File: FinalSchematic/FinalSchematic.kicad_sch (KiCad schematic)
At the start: 67 parts, among them M1 Pololu 4752, Q1 IRLZ44N, U1 OPA2197xD, U10 LM7912CT, U11 MEA1D1215SC, U12 OPA2197xD, U13 XR2206CP-F, U2 OPA2197xD, U3 OPA2197xD, U4 OPA2197xD, U5 LM311, U6 MCP1407-E_SN, U7 LM2917MX-8_NOPB, U8 OPA2197xD, U9 LM7812CT

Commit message: updated schematic
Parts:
- added RSHUNT: 1, symbol Device:R_US
- C11, C9: value 0.1u -> 1u
- C5: value 0.1u -> 0.027u
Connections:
- net GND: now also RSHUNT.1; no longer Q1.3 (S)
- new net: Q1.3 (S), RSHUNT.2
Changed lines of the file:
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@@
 	(wire
 		(pts
-			(xy 90.17 172.72) (xy 90.17 171.45)
-		)
-		(stroke
-			(width 0)
-			(type default)
-		)
-	)
-	(wire
-		(pts
 			(xy 127 76.2) (xy 124.46 76.2)
 		)
@@
 			)
 		)
-		(property "Value" "0.1u"
+		(property "Value" "0.027u"
 			(at 133.35 101.6 90)
 			(effects
@@
 	)
 	(symbol
+		(lib_id "Device:R_US")
+		(at 90.17 175.26 180)
+		(unit 1)
+		(exclude_from_sim no)
+		(in_bom yes)
+		(on_board yes)
+		(dnp no)
+		(fields_autoplaced yes)
+		(property "Reference" "RSHUNT"
+			(at 92.71 173.9899 0)
+			(effects
+				(font
+					(size 1.27 1.27)
+				)
+				(justify right)
+			)
+		)
+		(property "Value" "1"
+			(at 92.71 176.5299 0)
+			(effects
+				(font
+					(size 1.27 1.27)
+				)
+				(justify right)
+			)
+		)
+		(property "Footprint" ""
+			(at 89.154 175.006 90)
+			(effects
+				(font
+					(size 1.27 1.27)
+				)
+				(hide yes)
+			)
+		)
+		(property "Datasheet" "~"
+			(at 90.17 175.26 0)
+			(effects
+				(font
+					(size 1.27 1.27)
+				)
+				(hide yes)
+			)
+		)
+		(property "Description" "Resistor, US symbol"
+			(at 90.17 175.26 0)
+			(effects
+				(font
+					(size 1.27 1.27)
+				)
+				(hide yes)
+			)
+		)
+		(pin "2"
+		)
+		(pin "1"
+		)
+		(instances
+			(project "FinalSchematic"
+				(path "/3fb329af-5fd6-422e-bf74-f8f2d2cf8848"
+					(reference "RSHUNT")
+					(unit 1)
+				)
+			)
+		)
+	)
+	(symbol
 		(lib_id "Device:C_US")
 		(at 60.96 153.67 0)
@@
 			)
 		)
-		(property "Value" "0.1u"
+		(property "Value" "1u"
 			(at 265.43 134.112 90)
 			(effects
@@
 	(symbol
 		(lib_id "power:GND")
-		(at 90.17 172.72 0)
+		(at 90.17 179.07 0)
 		(unit 1)
 		(exclude_from_sim no)
@@
 		(fields_autoplaced yes)
 		(property "Reference" "#PWR016"
-			(at 90.17 179.07 0)
+			(at 90.17 185.42 0)
 			(effects
 				(font
@@
 		)
 		(property "Value" "GND"
-			(at 90.17 177.8 0)
+			(at 90.17 184.15 0)
 			(effects
 				(font
@@
 		)
 		(property "Footprint" ""
-			(at 90.17 172.72 0)
+			(at 90.17 179.07 0)
 			(effects
 				(font
@@
 		)
 		(property "Datasheet" ""
-			(at 90.17 172.72 0)
+			(at 90.17 179.07 0)
 			(effects
 				(font
@@
 		)
 		(property "Description" "Power symbol creates a global label with name \"GND\" , ground"
-			(at 90.17 172.72 0)
+			(at 90.17 179.07 0)
 			(effects
 				(font
@@
 			)
 		)
-		(property "Value" "0.1u"
+		(property "Value" "1u"
 			(at 173.736 127.254 0)
 			(effects

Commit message: updated schematic
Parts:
- removed RSHUNT: 1, symbol Device:R_US
- added R22: 100k, symbol Device:R_US
- renumbered Kp_Pot to PV37W104C01B00_A, Ki_Pot to PV37W104C01B00_B, FV_Pot to PV37W104C01B00_C, Bias_Pot to PV37W104C01B00_D
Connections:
- net GND: now also Q1.3 (S), R22.1
- net at R12.2, U8.6 (-): now also R22.2

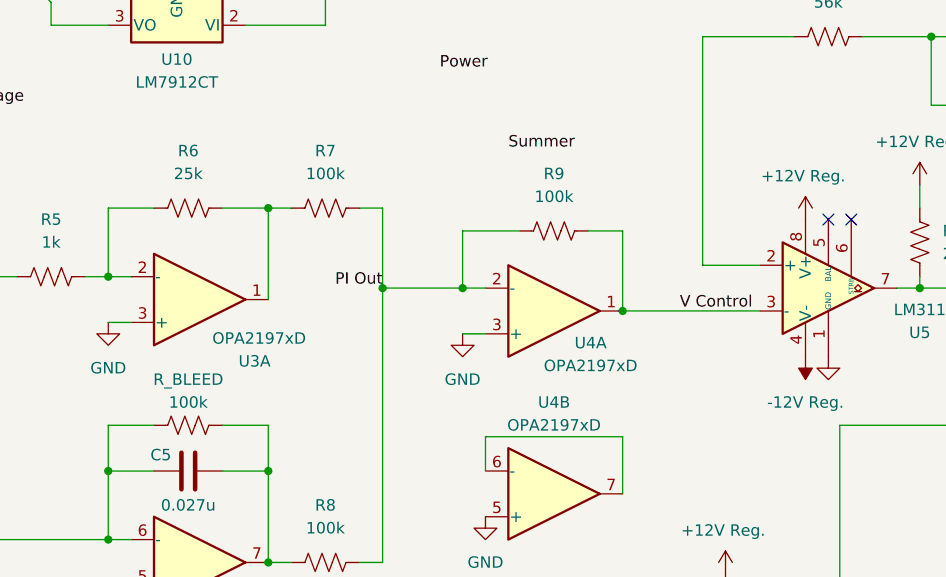
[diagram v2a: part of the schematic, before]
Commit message: updated schematic value, added block diagram.pdf
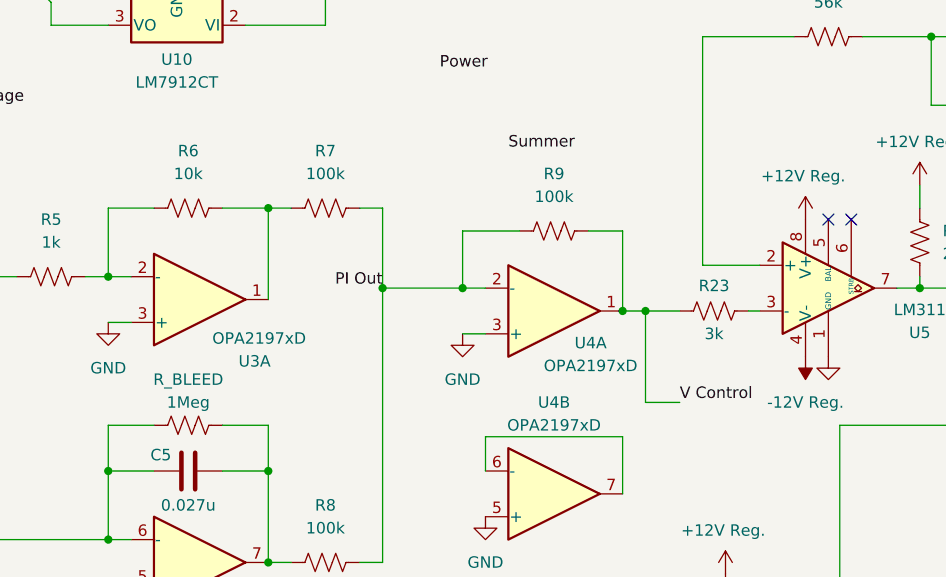
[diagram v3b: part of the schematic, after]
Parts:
- added R23: 3k, symbol Device:R_US
- R6: value 25k -> 10k
- R_BLEED: value 100k -> 1Meg
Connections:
- net V Control: now also R23.1; no longer U5.3 (-)
- new net: R23.2, U5.3 (-)
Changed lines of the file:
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@@
 	)
 	(junction
+		(at 184.15 80.01)
+		(diameter 0)
+		(color 0 0 0 0)
+	)
+	(junction
 		(at 246.38 46.99)
 		(diameter 0)
@@
 	(wire
 		(pts
+			(xy 195.58 80.01) (xy 196.85 80.01)
+		)
+		(stroke
+			(width 0)
+			(type default)
+		)
+	)
+	(wire
+		(pts
 			(xy 52.07 127) (xy 52.07 135.89)
 		)
@@
 	(wire
 		(pts
+			(xy 184.15 90.17) (xy 187.96 90.17)
+		)
+		(stroke
+			(width 0)
+			(type default)
+		)
+	)
+	(wire
+		(pts
 			(xy 80.01 38.1) (xy 80.01 40.64)
 		)
@@
 	(wire
 		(pts
-			(xy 181.61 80.01) (xy 196.85 80.01)
+			(xy 181.61 80.01) (xy 184.15 80.01)
 		)
 		(stroke
@@
 	(wire
 		(pts
+			(xy 184.15 90.17) (xy 184.15 80.01)
+		)
+		(stroke
+			(width 0)
+			(type default)
+		)
+	)
+	(wire
+		(pts
 			(xy 86.36 63.5) (xy 88.9 63.5)
 		)
@@
 	(wire
 		(pts
+			(xy 184.15 80.01) (xy 187.96 80.01)
+		)
+		(stroke
+			(width 0)
+			(type default)
+		)
+	)
+	(wire
+		(pts
 			(xy 100.33 124.46) (xy 120.65 124.46)
 		)
@@
 	)
 	(label "V Control"
-		(at 187.96 80.01 0)
+		(at 187.96 90.17 0)
 		(effects
 			(font
@@
 			)
 		)
-		(property "Value" "100k"
+		(property "Value" "1Meg"
 			(at 133.35 90.17 90)
 			(effects
@@
 	(symbol
 		(lib_id "Device:R_US")
+		(at 191.77 80.01 90)
+		(unit 1)
+		(exclude_from_sim no)
+		(in_bom yes)
+		(on_board yes)
+		(dnp no)
+		(property "Reference" "R23"
+			(at 191.77 77.216 90)
+			(effects
+				(font
+					(size 1.27 1.27)
+				)
+			)
+		)
+		(property "Value" "3k"
+			(at 191.77 82.55 90)
+			(effects
+				(font
+					(size 1.27 1.27)
+				)
+			)
+		)
+		(property "Footprint" ""
+			(at 192.024 78.994 90)
+			(effects
+				(font
+					(size 1.27 1.27)
+				)
+				(hide yes)
+			)
+		)
+		(property "Datasheet" "~"
+			(at 191.77 80.01 0)
+			(effects
+				(font
+					(size 1.27 1.27)
+				)
+				(hide yes)
+			)
+		)
+		(property "Description" "Resistor, US symbol"
+			(at 191.77 80.01 0)
+			(effects
+				(font
+					(size 1.27 1.27)
+				)
+				(hide yes)
+			)
+		)
+		(pin "2"
+		)
+		(pin "1"
+		)
+		(instances
+			(project "FinalSchematic"
+				(path "/3fb329af-5fd6-422e-bf74-f8f2d2cf8848"
+					(reference "R23")
+					(unit 1)
+				)
+			)
+		)
+	)
+	(symbol
+		(lib_id "Device:R_US")
 		(at 193.04 123.19 180)
 		(unit 1)
@@
 			)
 		)
-		(property "Value" "25k"
+		(property "Value" "10k"
 			(at 133.35 64.77 90)
 			(effects

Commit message: final schematic update
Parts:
- added C24, C25: 0.1u, symbol Device:C_Small
- added C26: 0.027u, symbol Device:C
- added PV37W104C01B00_A1, PV37W104C01B00_B1: 100k, symbol Device:R_Potentiometer_US
- added R24, R26, R27: 10k, symbol Device:R_US
- added R25: 1k, symbol Device:R_US
- added R28, R29: 100k, symbol Device:R_US
- added R_BLEED1: 1Meg, symbol Device:R_US
- added U14: OPA2197xD, Package_SO:SOIC-8_3.9x4.9mm_P1.27mm, symbol Amplifier_Operational:OPA2197xD
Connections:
- net +12V Reg.: now also C1.1, C13.1, C14.1, C15.1, C16.1, C3.1, U1.8 (V+), U12.8 (V+), U2.8 (V+), U3.8 (V+), U4.8 (V+), U8.8 (V+), C24.1, U14.8 (V+)
- net -12V Reg.: now also C17.1, C18.1, C19.1, C2.1, C20.1, C4.1, U1.4 (V-), U10.3 (VO), U12.4 (V-), U2.4 (V-), U3.4 (V-), U4.4 (V-), U8.4 (V-), C25.1, U14.4 (V-)
- net GND: now also C24.2, C25.2, U14.3 (+), U14.5 (+); no longer PV37W104C01B00_A.3, PV37W104C01B00_B.3, R18.1, R19.1
- net at C5.1, R_BLEED.1, U3.6 (-): now also R24.2; no longer PV37W104C01B00_B.2
- net at PV37W104C01B00_A.2, R5.1: now also PV37W104C01B00_A.3
- new net: PV37W104C01B00_B1.2, PV37W104C01B00_B1.3, R26.1
- new net: PV37W104C01B00_B.2, PV37W104C01B00_B.3, R24.1
- new net: PV37W104C01B00_A1.2, PV37W104C01B00_A1.3, R25.1
- new net: R25.2, R27.1, U14.2 (-)
- new net: R27.2, R28.1, U14.1
- new net: C26.1, R26.2, R_BLEED1.1, U14.6 (-)
- new net: C26.2, R29.1, R_BLEED1.2, U14.7
- new net: R18.1, R19.1
- new net V_{c}: R28.2, R29.2
- new net V_{e}: PV37W104C01B00_A1.1, PV37W104C01B00_B1.1
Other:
- moved on the sheet: C1, C13, C14, C15, C16, C17, C18, C19, C2, C20, C3, C4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

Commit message: measurements
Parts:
- added R30: 100k, symbol Device:R_US
- C5: value 0.027u -> 0.47u
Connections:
- net GND: now also R30.2
- net at PV37W104C01B00_C.1: now also R30.1
- no-connect marks 9 -> 8
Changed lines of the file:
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@@
 		(at 257.81 118.11)
 	)
-	(no_connect
-		(at 143.51 135.89)
-	)
 	(bus_entry
 		(at 115.57 15.24)
@@
 	(wire
 		(pts
+			(xy 144.78 128.27) (xy 148.59 128.27)
+		)
+		(stroke
+			(width 0)
+			(type default)
+		)
+	)
+	(wire
+		(pts
 			(xy 57.15 116.84) (xy 57.15 113.03)
 		)
@@
 	(wire
 		(pts
+			(xy 143.51 135.89) (xy 148.59 135.89)
+		)
+		(stroke
+			(width 0)
+			(type default)
+		)
+	)
+	(wire
+		(pts
 			(xy 124.46 48.26) (xy 118.11 48.26)
 		)
@@
 		(on_board yes)
 		(dnp no)
-		(fields_autoplaced yes)
 		(property "Reference" "PV37W104C01B00_C"
-			(at 139.7 129.54 90)
+			(at 133.35 129.54 90)
 			(effects
 				(font
@@
 			)
 		)
-		(property "Value" "0.027u"
+		(property "Value" "0.47u"
 			(at 133.35 101.6 90)
 			(effects
@@
 	(symbol
 		(lib_id "power:GND")
+		(at 144.78 128.27 0)
+		(unit 1)
+		(exclude_from_sim no)
+		(in_bom yes)
+		(on_board yes)
+		(dnp no)
+		(property "Reference" "#PWR072"
+			(at 144.78 134.62 0)
+			(effects
+				(font
+					(size 1.27 1.27)
+				)
+				(hide yes)
+			)
+		)
+		(property "Value" "GND"
+			(at 144.78 132.08 0)
+			(effects
+				(font
+					(size 1.27 1.27)
+				)
+			)
+		)
+		(property "Footprint" ""
+			(at 144.78 128.27 0)
+			(effects
+				(font
+					(size 1.27 1.27)
+				)
+				(hide yes)
+			)
+		)
+		(property "Datasheet" ""
+			(at 144.78 128.27 0)
+			(effects
+				(font
+					(size 1.27 1.27)
+				)
+				(hide yes)
+			)
+		)
+		(property "Description" "Power symbol creates a global label with name \"GND\" , ground"
+			(at 144.78 128.27 0)
+			(effects
+				(font
+					(size 1.27 1.27)
+				)
+				(hide yes)
+			)
+		)
+		(pin "1"
+		)
+		(instances
+			(project "FinalSchematic"
+				(path "/3fb329af-5fd6-422e-bf74-f8f2d2cf8848"
+					(reference "#PWR072")
+					(unit 1)
+				)
+			)
+		)
+	)
+	(symbol
+		(lib_id "power:GND")
 		(at 262.89 123.19 0)
 		(unit 1)
@@
 					(unit 1)
 				)
+			)
+		)
+	)
+	(symbol
+		(lib_id "Device:R_US")
+		(at 148.59 132.08 180)
+		(unit 1)
+		(exclude_from_sim no)
+		(in_bom yes)
+		(on_board yes)
+		(dnp no)
+		(property "Reference" "R30"
+			(at 152.4 130.048 0)
+			(effects
+				(font
+					(size 1.27 1.27)
+				)
+			)
+		)
+		(property "Value" "100k"
+			(at 152.4 132.08 0)
+			(effects
+				(font
+					(size 1.27 1.27)
+				)
+			)
+		)
+		(property "Footprint" ""
+			(at 147.574 131.826 90)
+			(effects
+				(font
+					(size 1.27 1.27)
+				)
+				(hide yes)
+			)
+		)
+		(property "Datasheet" "~"
+			(at 148.59 132.08 0)
+			(effects
+				(font
+					(size 1.27 1.27)
+				)
+				(hide yes)
+			)
+		)
+		(property "Description" "Resistor, US symbol"
+			(at 148.59 132.08 0)
+			(effects
+				(font
+					(size 1.27 1.27)
+				)
+				(hide yes)
+			)
+		)
+		(pin "2"
+		)
+		(pin "1"
+		)
+		(instances
+			(project "FinalSchematic"
+				(path "/3fb329af-5fd6-422e-bf74-f8f2d2cf8848"
+					(reference "R30")
+					(unit 1)
+				)

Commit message: adsf
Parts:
- removed C24, C25: 0.1u, symbol Device:C_Small
- added BT1, BT2: Battery_Cell, symbol Device:Battery_Cell
- added C24, C25: 0.1u, symbol Device:C
- added C27, C28, C29, C30: 0.1u, symbol Device:C_Small
- added L: L, symbol Device:L
- added PV37W104C01B00_C1: 100k, symbol Device:R_Potentiometer_US
- added R, R31, R32: 100k, symbol Device:R_US
- added R33: 470, symbol Device:R_US
- added U15, U16, U17: OPA2197xD, Package_SO:SOIC-8_3.9x4.9mm_P1.27mm, symbol Amplifier_Operational:OPA2197xD
- added U18: LM2917MX-8_NOPB, LM2917MX-8_NOPB:SOIC127P599X175-8N, symbol LM2917MX-8_NOPB:LM2917MX-8_NOPB
- C26: value 0.027u -> 0.47u
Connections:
- net +12V Reg.: now also C27.1, C29.1, R33.2, U15.8 (V+), U16.8 (V+), U17.8 (V+), U18.5 (COL)
- net -12V Reg.: now also C28.1, C30.1, U15.4 (V-), U16.4 (V-), U17.4 (V-)
- net GND: now also C24.2, C25.2, C27.2, C28.2, C29.2, C30.2, PV37W104C01B00_C1.3, R32.2, U15.3 (+), U15.5 (+), U18.8 (TACH-/GND)
- net PI Out: now also R31.1, U15.2 (-)
- net V Control: now also R31.2, U15.1
- net V_{c} renamed PI_{out}
- new net: BT2.1 (+), R.1
- new net: L.2, R.2
- new net: U15.6 (-), U15.7
- new net: BT1.1 (+), L.1
- new net: BT1.2 (-), BT2.2 (-)
- new net: C24.1, PV37W104C01B00_C1.2, U18.3 (CP2/IN+)
- new net: PV37W104C01B00_C1.1, R32.1
- new net: C25.1, U18.2 (CP1)
- new net: U18.4 (EMIT), U18.7 (IN-)
- new net: R33.1, U18.6 (V+)

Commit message: ghhkj
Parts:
- added U19, U20, U21, U22, U23, U24: OPA2197xD, Package_SO:SOIC-8_3.9x4.9mm_P1.27mm, symbol Amplifier_Operational:OPA2197xD
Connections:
- net +12V Reg.: now also U19.8 (V+), U20.8 (V+), U21.8 (V+), U22.8 (V+), U23.8 (V+), U24.8 (V+)
- net -12V Reg.: now also U19.4 (V-), U20.4 (V-), U21.4 (V-), U22.4 (V-), U23.4 (V-), U24.4 (V-)
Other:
- moved on the sheet: R12, R14, R6, R9
